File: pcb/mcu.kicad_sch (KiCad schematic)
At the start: 5 parts, among them J1 Conn_01x04, SW1 TS02-66-43-BK-160-LCR-D, U2 AVR16DD20-I/SO

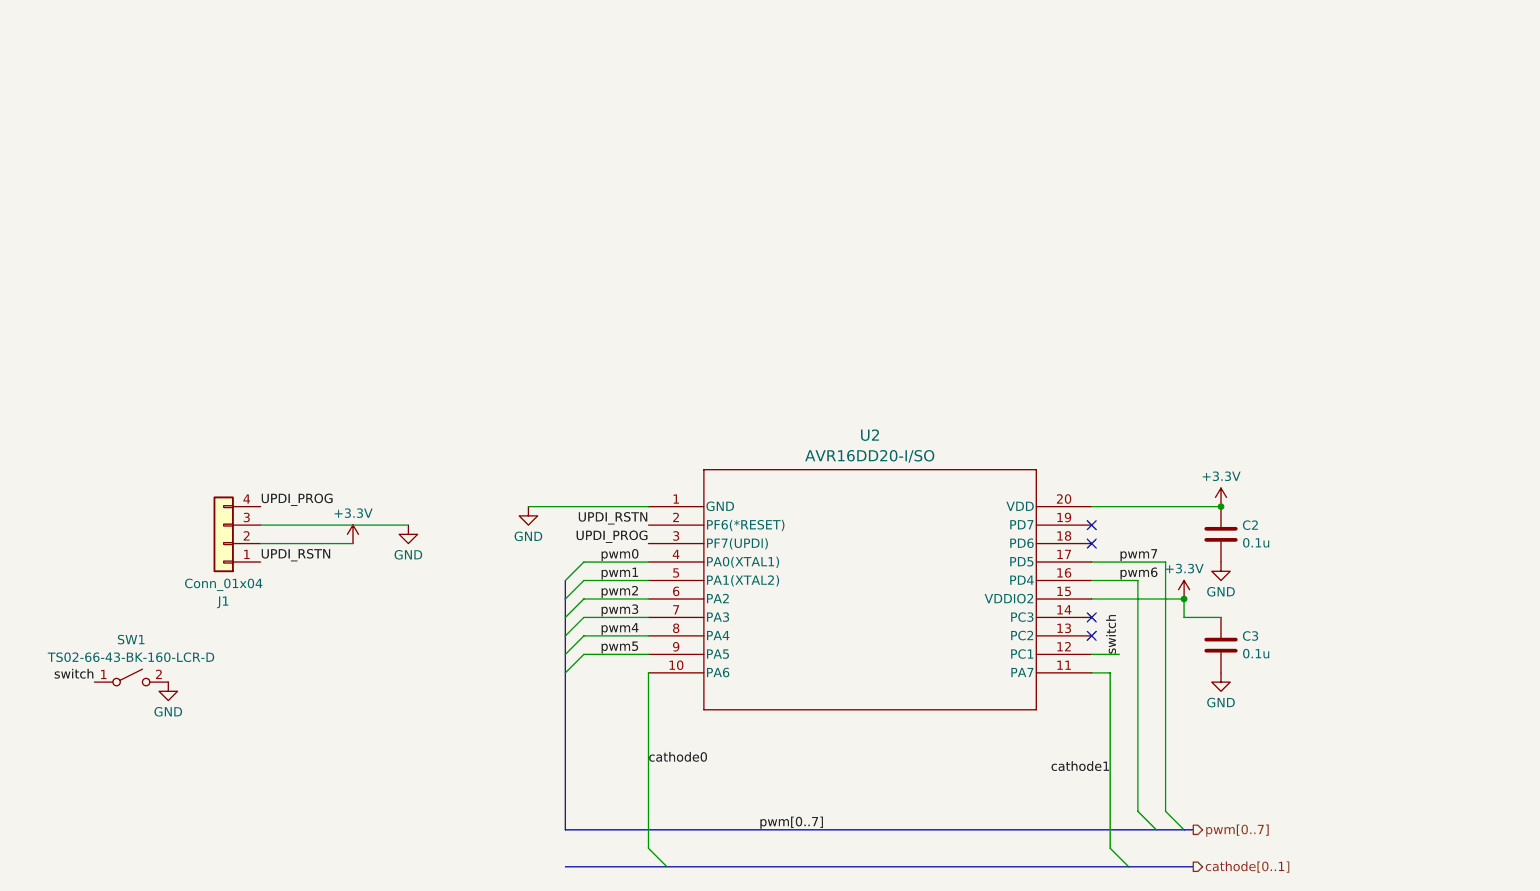
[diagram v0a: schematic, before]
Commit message: Swap to STC8H1K08 and work on JLCPCB assembly support
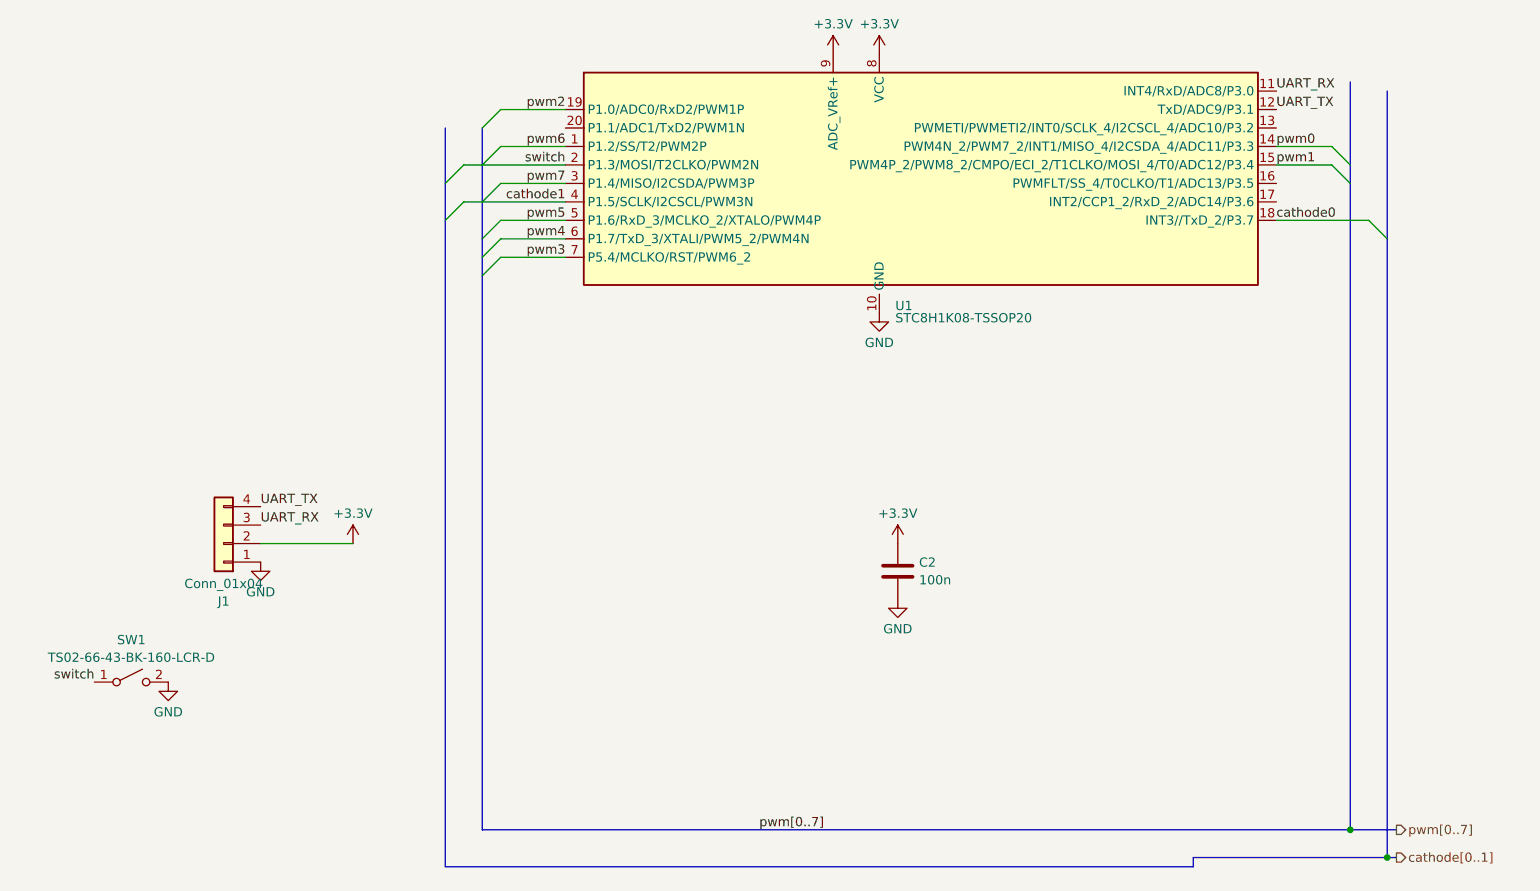
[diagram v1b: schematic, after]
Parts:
- removed C3: 0.1u, Capacitor_SMD:C_0603_1608Metric_Pad1.08x0.95mm_HandSolder, symbol Device:C
- removed U2: AVR16DD20-I/SO, Package_SO:SOIC-20W_7.5x12.8mm_P1.27mm, symbol AVR16:AVR16DD20-I_SO
- added U1: STC8H1K08-TSSOP20, Package_SO:TSSOP-20_4.4x6.5mm_P0.65mm, symbol stc8h:STC8H1K08
- C2: value 0.1u -> 100n; LCSC (none) -> C1525
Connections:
- net UPDI_RSTN is gone; now on net GND: J1.1 (Pin_1)
- net +3.3V: now also U1.8 (VCC), U1.9 (ADC_VRef+)
- net GND: now also U1.10 (GND); no longer J1.3 (Pin_3)
- net cathode0: now also U1.18 (INT3//TxD_2/P3.7)
- net cathode1: now also U1.4 (P1.5/SCLK/I2CSCL/PWM3N)
- net pwm0: now also U1.14 (PWM4N_2/PWM7_2/INT1/MISO_4/I2CSDA_4/ADC11/P3.3)
- net pwm1: now also U1.15 (PWM4P_2/PWM8_2/CMPO/ECI_2/T1CLKO/MOSI_4/T0/ADC12/P3.4)
- net pwm2: now also U1.19 (P1.0/ADC0/RxD2/PWM1P)
- net pwm3: now also U1.7 (P5.4/MCLKO/RST/PWM6_2)
- net pwm4: now also U1.6 (P1.7/TxD_3/XTALI/PWM5_2/PWM4N)
- net pwm5: now also U1.5 (P1.6/RxD_3/MCLKO_2/XTALO/PWM4P)
- net pwm6: now also U1.1 (P1.2/SS/T2/PWM2P)
- net pwm7: now also U1.3 (P1.4/MISO/I2CSDA/PWM3P)
- net switch: now also U1.2 (P1.3/MOSI/T2CLKO/PWM2N)
- net UPDI_PROG renamed UART_TX
- net UART_TX: now also U1.12 (TxD/ADC9/P3.1)
- new net UART_RX: J1.3 (Pin_3), U1.11 (INT4/RxD/ADC8/P3.0)
- no-connect marks 4 -> 0

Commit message: More edits to PCB design
 - Change a couple of parts - voltage regulator - to use LCSC parts
 - Increase width of the nametag PCB
 - redo layout a bit
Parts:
- SW1: value TS02-66-43-BK-160-LCR-D -> TS-1088-AR02016; footprint Button_Switch_THT:SW_PUSH_6mm_H4.3mm -> Button_Switch_SMD:SW_Push_SPST_NO_Alps_SKRK
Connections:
- net pwm0: now also U1.20 (P1.1/ADC1/TxD2/PWM1N); no longer U1.14 (PWM4N_2/PWM7_2/INT1/MISO_4/I2CSDA_4/ADC11/P3.3)
- net pwm2: now also U1.3 (P1.4/MISO/I2CSDA/PWM3P); no longer U1.19 (P1.0/ADC0/RxD2/PWM1P)
- net pwm4: now also U1.19 (P1.0/ADC0/RxD2/PWM1P); no longer U1.6 (P1.7/TxD_3/XTALI/PWM5_2/PWM4N)
- net pwm7: now also U1.14 (PWM4N_2/PWM7_2/INT1/MISO_4/I2CSDA_4/ADC11/P3.3); no longer U1.3 (P1.4/MISO/I2CSDA/PWM3P)

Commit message: Update PCB to reflect PWM pin assignments
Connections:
- net pwm0: now also U1.7 (P5.4/MCLKO/RST/PWM6_2); no longer U1.20 (P1.1/ADC1/TxD2/PWM1N)
- net pwm3: now also U1.6 (P1.7/TxD_3/XTALI/PWM5_2/PWM4N); no longer U1.7 (P5.4/MCLKO/RST/PWM6_2)
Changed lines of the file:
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@@
 	)
 	(bus_entry
-		(at 86.36 33.02)
+		(at 86.36 48.26)
 		(size 2.54 -2.54)
 		(stroke
@@
 	(wire
 		(pts
-			(xy 88.9 30.48) (xy 97.79 30.48)
+			(xy 88.9 45.72) (xy 97.79 45.72)
 		)
 		(stroke
@@
 	)
 	(label "pwm3"
-		(at 97.79 48.26 180)
+		(at 97.79 45.72 180)
 		(effects
 			(font
@@
 	)
 	(label "pwm0"
-		(at 97.79 30.48 180)
-		(effects
-			(font
+		(at 97.79 48.26 180)
+		(effects
+			(font

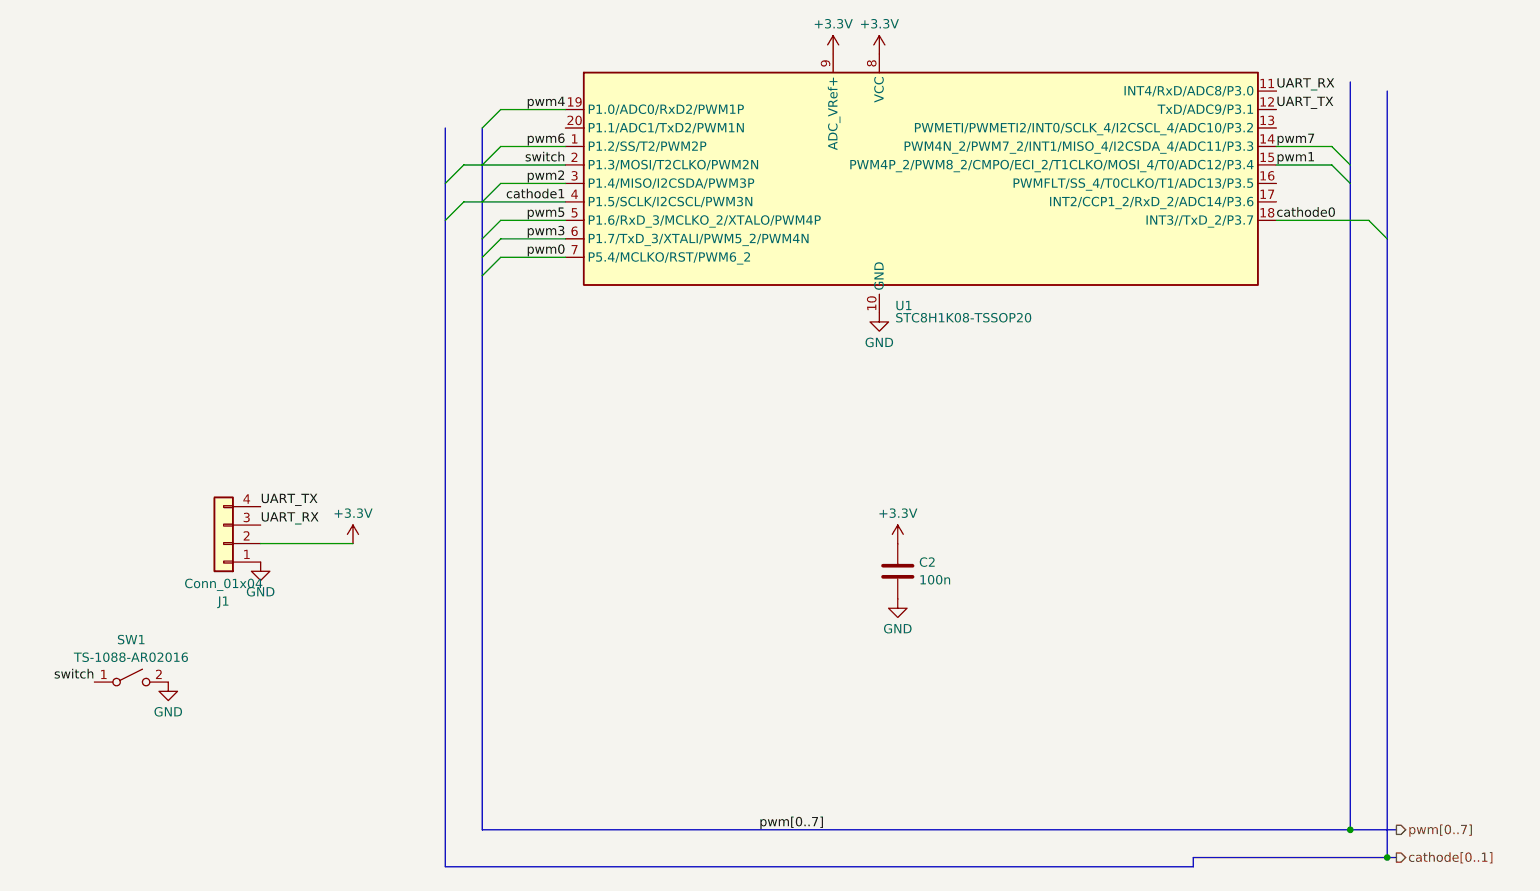
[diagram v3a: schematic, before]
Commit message: Update PCB with new naming of PWM channels
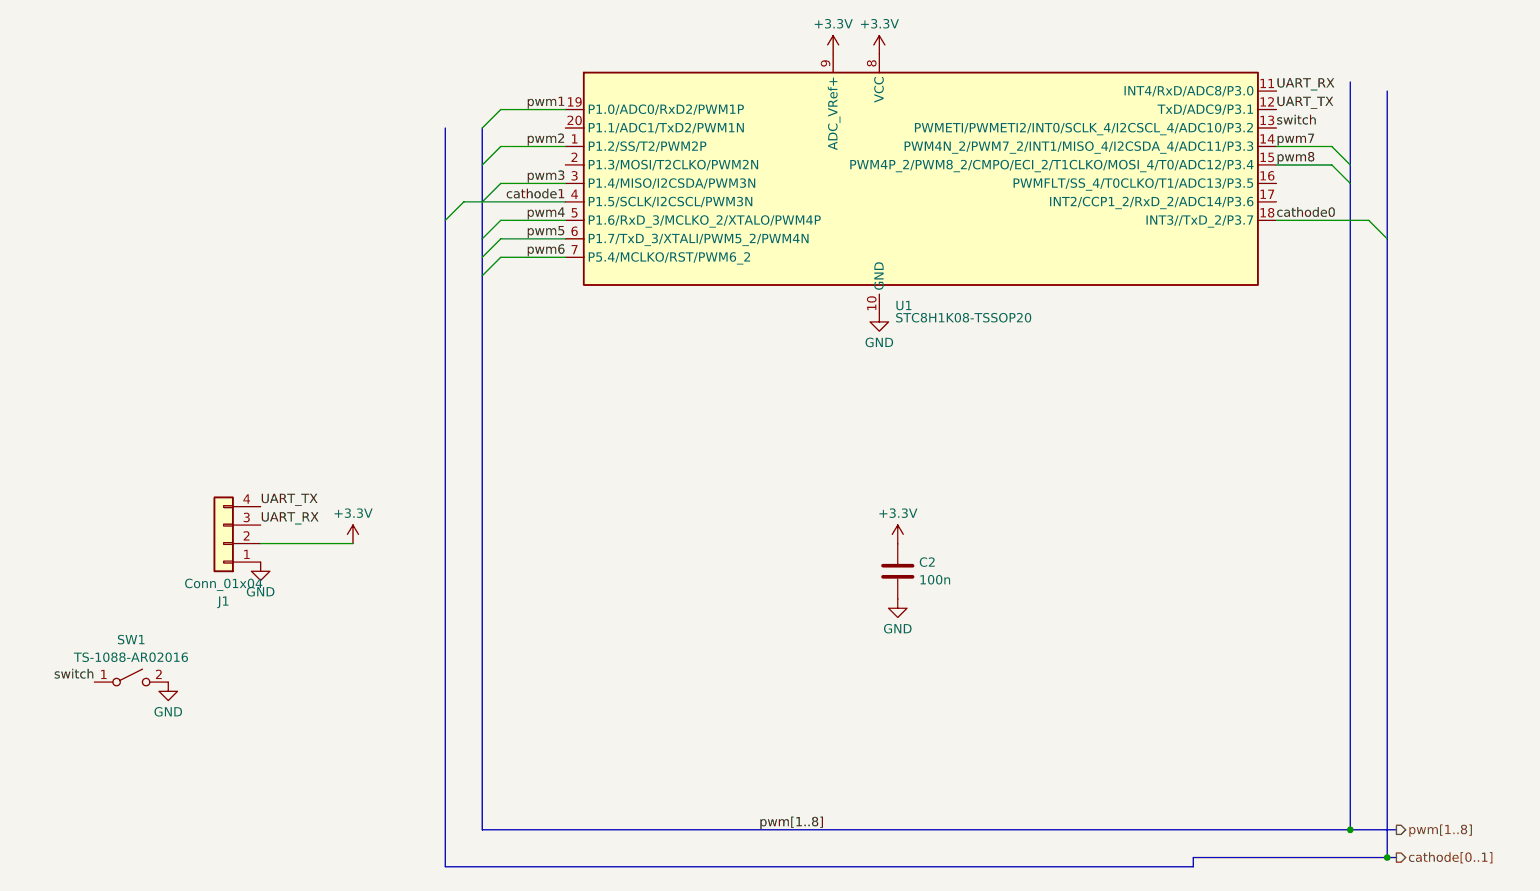
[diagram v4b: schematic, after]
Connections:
- net pwm0 is gone; now on net pwm6: U1.7 (P5.4/MCLKO/RST/PWM6_2)
- net pwm1: now also U1.19 (P1.0/ADC0/RxD2/PWM1P); no longer U1.15 (PWM4P_2/PWM8_2/CMPO/ECI_2/T1CLKO/MOSI_4/T0/ADC12/P3.4)
- net pwm2: now also U1.1 (P1.2/SS/T2/PWM2P); no longer U1.3 (P1.4/MISO/I2CSDA/PWM3P)
- net pwm3: now also U1.3 (P1.4/MISO/I2CSDA/PWM3N); no longer U1.6 (P1.7/TxD_3/XTALI/PWM5_2/PWM4N)
- net pwm4: now also U1.5 (P1.6/RxD_3/MCLKO_2/XTALO/PWM4P); no longer U1.19 (P1.0/ADC0/RxD2/PWM1P)
- net pwm5: now also U1.6 (P1.7/TxD_3/XTALI/PWM5_2/PWM4N); no longer U1.5 (P1.6/RxD_3/MCLKO_2/XTALO/PWM4P)
- net pwm6: no longer U1.1 (P1.2/SS/T2/PWM2P)
- net switch: now also U1.13 (PWMETI/PWMETI2/INT0/SCLK_4/I2CSCL_4/ADC10/P3.2); no longer U1.2 (P1.3/MOSI/T2CLKO/PWM2N)
- new net pwm8: U1.15 (PWM4P_2/PWM8_2/CMPO/ECI_2/T1CLKO/MOSI_4/T0/ADC12/P3.4)
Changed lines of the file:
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@@
-	)
-	(bus_entry
-		(at 81.28 38.1)
-		(size 2.54 -2.54)
-		(stroke
-			(width 0)
-			(type default)
-		)
 	)
 	(bus_entry
@@
 		)
 	)
-	(wire
-		(pts
-			(xy 86.36 35.56) (xy 97.79 35.56)
-		)
-		(stroke
-			(width 0)
-			(type default)
-		)
-	)
 	(bus
 		(pts
@@
 	(wire
 		(pts
-			(xy 83.82 35.56) (xy 86.36 35.56)
-		)
-		(stroke
-			(width 0)
-			(type default)
-		)
-	)
-	(wire
-		(pts
 			(xy 88.9 45.72) (xy 97.79 45.72)
 		)
@@
 	(bus
 		(pts
-			(xy 81.28 38.1) (xy 81.28 43.18)
+			(xy 81.28 30.48) (xy 81.28 43.18)
 		)
 		(stroke
@@
 		(pts
 			(xy 205.74 38.1) (xy 205.74 127)
-		)
-		(stroke
-			(width 0)
-			(type default)
-		)
-	)
-	(bus
-		(pts
-			(xy 81.28 30.48) (xy 81.28 38.1)
 		)
 		(stroke
@@
 		)
 	)
-	(label "pwm5"
+	(label "pwm4"
 		(at 97.79 43.18 180)
 		(effects
@@
 		)
 	)
-	(label "pwm2"
+	(label "pwm3"
 		(at 97.79 38.1 180)
 		(effects
@@
 		)
 	)
-	(label "pwm4"
+	(label "pwm1"
 		(at 97.79 27.94 180)
 		(effects
@@
 		)
 	)
+	(label "pwm2"
+		(at 97.79 33.02 180)
+		(effects
+			(font
+				(size 1.27 1.27)
+			)
+			(justify right bottom)
+		)
+	)
+	(label "pwm5"
+		(at 97.79 45.72 180)
+		(effects
+			(font
+				(size 1.27 1.27)
+			)
+			(justify right bottom)
+		)
+	)
+	(label "pwm[1..8]"
+		(at 124.46 127 0)
+		(effects
+			(font
+				(size 1.27 1.27)
+			)
+			(justify left bottom)
+		)
+	)
 	(label "pwm6"
-		(at 97.79 33.02 180)
-		(effects
-			(font
-				(size 1.27 1.27)
-			)
-			(justify right bottom)
-		)
-	)
-	(label "pwm3"
-		(at 97.79 45.72 180)
-		(effects
-			(font
-				(size 1.27 1.27)
-			)
-			(justify right bottom)
-		)
-	)
-	(label "pwm[0..7]"
-		(at 124.46 127 0)
-		(effects
-			(font
-				(size 1.27 1.27)
-			)
-			(justify left bottom)
-		)
-	)
-	(label "pwm0"
 		(at 97.79 48.26 180)
 		(effects
@@
 		)
 	)
-	(label "pwm1"
+	(label "pwm8"
 		(at 195.58 35.56 0)
 		(effects
@@
 	)
 	(label "switch"
-		(at 97.79 35.56 180)
-		(effects
-			(font
-				(size 1.27 1.27)
-			)
-			(justify right bottom)
+		(at 195.58 30.48 0)
+		(effects
+			(font
+				(size 1.27 1.27)
+			)
+			(justify left bottom)
 		)
 	)
@@
 		)
 	)
-	(hierarchical_label "pwm[0..7]"
+	(hierarchical_label "pwm[1..8]"
 		(shape output)
 		(at 212.09 127 0)

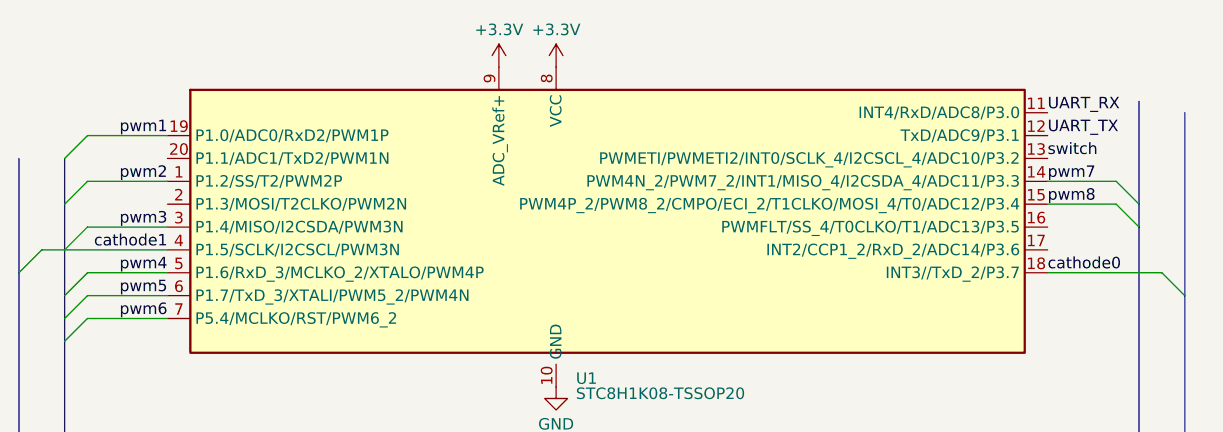
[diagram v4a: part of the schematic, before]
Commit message: Small changes for manufacturability
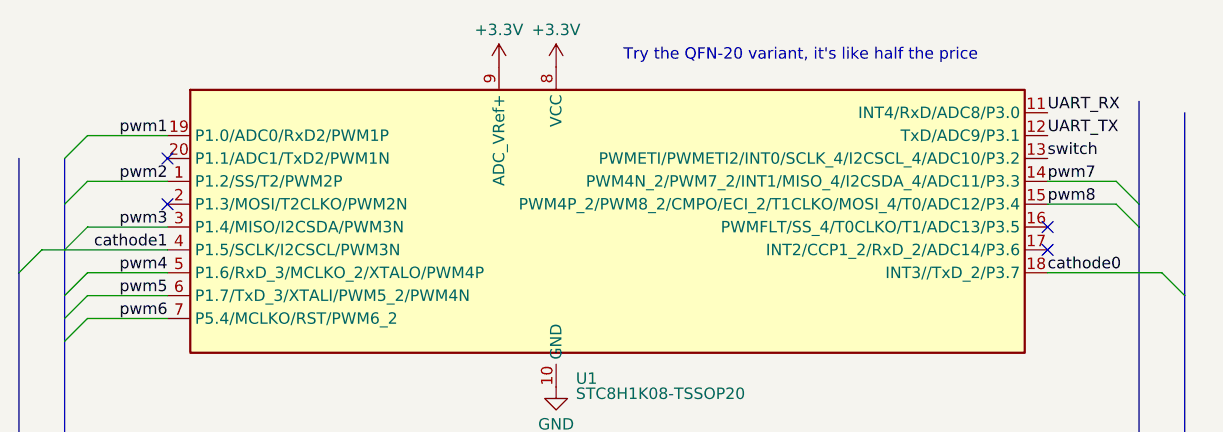
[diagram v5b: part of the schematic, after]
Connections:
- no-connect marks 0 -> 4
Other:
- note added: "Try the QFN-20 variant, it's like half the price"
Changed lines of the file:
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@@
 	(generator_version "10.0")
 	(paper "A4")
+	(text "Try the QFN-20 variant, it's like half the price"
+		(exclude_from_sim no)
+		(at 168.148 19.05 0)
+		(effects
+			(font
+				(size 1.27 1.27)
+			)
+		)
+	)
 	(junction
 		(at 205.74 127)
@@
 		(color 0 0 0 0)
 	)
+	(no_connect
+		(at 195.58 38.1)
+	)
+	(no_connect
+		(at 97.79 35.56)
+	)
+	(no_connect
+		(at 195.58 40.64)
+	)
+	(no_connect
+		(at 97.79 30.48)
+	)
 	(bus_entry
